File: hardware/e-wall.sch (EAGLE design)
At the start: 52 parts, among them IC1 74HCT595D, IC2 74HCT595D, IC3 74HCT595D, Q1 BSS123, Q10 BSS123, Q11 BSS123, Q12 BSS123, Q13 BSS123, Q14 BSS123, Q15 BSS123, Q16 BSS123, Q17 BSS123, Q18 BSS123, Q19 BSS123, Q2 BSS123, Q20 BSS123, Q21 BSS123, Q22 BSS123, Q23 BSS123, Q24 BSS123, Q3 BSS123, Q4 BSS123, Q5 BSS123, Q6 BSS123, Q7 BSS123, Q8 BSS123, Q9 BSS123

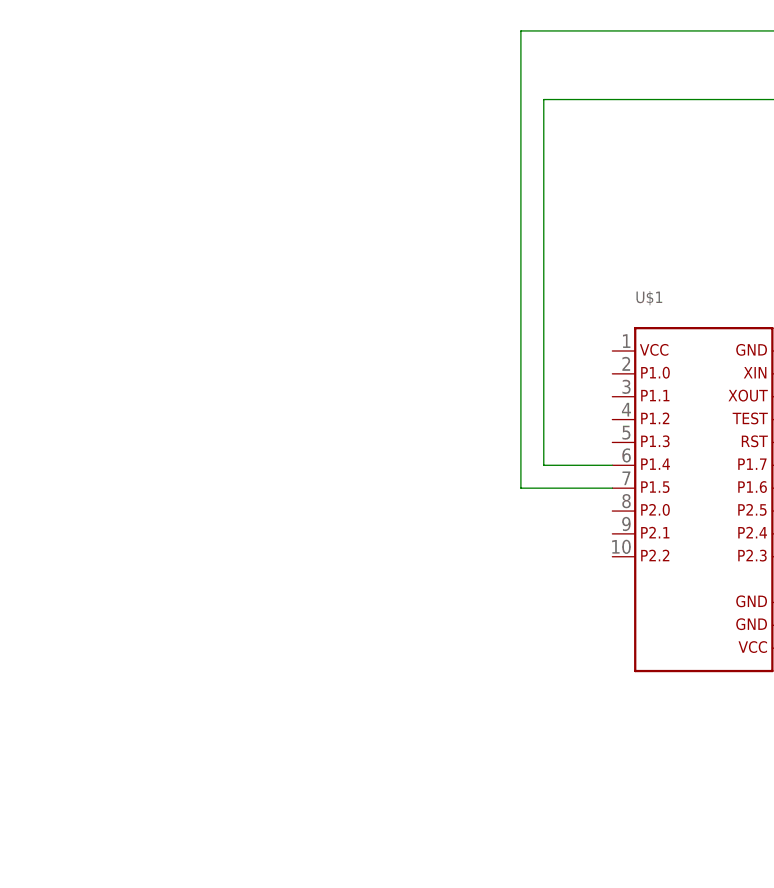
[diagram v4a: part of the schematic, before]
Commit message: Pegelwandler für Ultraschallsensor gezeichnet, aber noch nicht dimensioniert
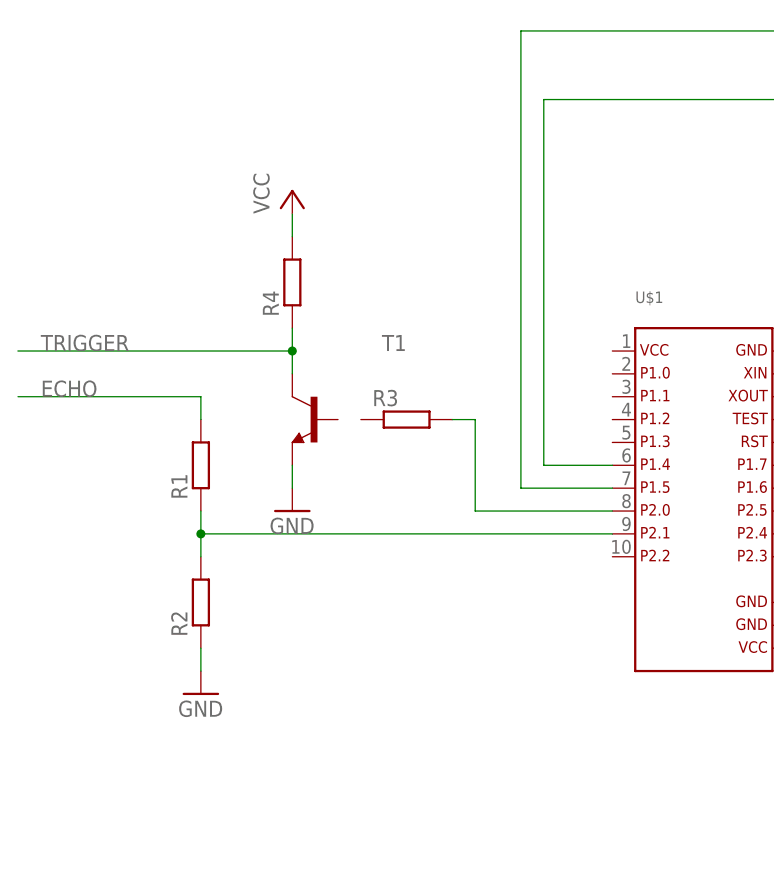
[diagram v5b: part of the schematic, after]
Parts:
- added R1, R2, R3, R4: (no value), resistor:R-EU_R0805
- added T1: (no value), transistor:-NPN-SOT23-EBC
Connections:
- new net ECHO: R1.2
- new net N$31: R1.1, R2.2, U$1.9
- new net N$32: R3.2, U$1.8
- new net TRIGGER: R4.1, T1.C
- net GND: now also R2.1, T1.E
- net VCC: now also R4.2
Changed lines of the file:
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@@
 <part name="P+26" library="supply1" deviceset="+12V" device=""/>
 <part name="P+27" library="supply1" deviceset="+12V" device=""/>
+<part name="R1" library="resistor" deviceset="R-EU_" device="R0805"/>
+<part name="R2" library="resistor" deviceset="R-EU_" device="R0805"/>
+<part name="R3" library="resistor" deviceset="R-EU_" device="R0805"/>
+<part name="R4" library="resistor" deviceset="R-EU_" device="R0805"/>
+<part name="T1" library="transistor" deviceset="*-NPN-" device="SOT23-EBC"/>
+<part name="GND28" library="supply1" deviceset="GND" device=""/>
+<part name="GND29" library="supply1" deviceset="GND" device=""/>
+<part name="P+28" library="supply1" deviceset="VCC" device=""/>
 </parts>
 <sheets>
@@
 <instance part="P+26" gate="1" x="447.04" y="68.58"/>
 <instance part="P+27" gate="1" x="447.04" y="43.18"/>
+<instance part="R1" gate="G$1" x="22.86" y="60.96" rot="R90"/>
+<instance part="R2" gate="G$1" x="22.86" y="45.72" rot="R90"/>
+<instance part="R3" gate="G$1" x="45.72" y="66.04"/>
+<instance part="R4" gate="G$1" x="33.02" y="81.28" rot="R90"/>
+<instance part="T1" gate="G$1" x="35.56" y="66.04" rot="MR0"/>
+<instance part="GND28" gate="1" x="33.02" y="55.88"/>
+<instance part="GND29" gate="1" x="22.86" y="35.56"/>
+<instance part="P+28" gate="VCC" x="33.02" y="91.44"/>
 </instances>
 <busses>
@@
 <pinref part="GND24" gate="1" pin="GND"/>
 <wire x1="439.42" y1="17.78" x2="439.42" y2="20.32" width="0.1524" layer="91"/>
+</segment>
+<segment>
+<pinref part="R2" gate="G$1" pin="1"/>
+<pinref part="GND29" gate="1" pin="GND"/>
+<wire x1="22.86" y1="40.64" x2="22.86" y2="38.1" width="0.1524" layer="91"/>
+</segment>
+<segment>
+<pinref part="T1" gate="G$1" pin="E"/>
+<pinref part="GND28" gate="1" pin="GND"/>
+<wire x1="33.02" y1="58.42" x2="33.02" y2="60.96" width="0.1524" layer="91"/>
 </segment>
 </net>
@@
 <pinref part="P+3" gate="VCC" pin="VCC"/>
 </segment>
+<segment>
+<pinref part="P+28" gate="VCC" pin="VCC"/>
+<pinref part="R4" gate="G$1" pin="2"/>
+<wire x1="33.02" y1="88.9" x2="33.02" y2="86.36" width="0.1524" layer="91"/>
+</segment>
 </net>
 <net name="OUT0" class="0">
@@
 </segment>
 </net>
+<net name="N$31" class="0">
+<segment>
+<pinref part="R1" gate="G$1" pin="1"/>
+<pinref part="R2" gate="G$1" pin="2"/>
+<wire x1="22.86" y1="55.88" x2="22.86" y2="53.34" width="0.1524" layer="91"/>
+<pinref part="U$1" gate="G$1" pin="9"/>
+<wire x1="22.86" y1="53.34" x2="22.86" y2="50.8" width="0.1524" layer="91"/>
+<wire x1="22.86" y1="53.34" x2="68.58" y2="53.34" width="0.1524" layer="91"/>
+<junction x="22.86" y="53.34"/>
+</segment>
+</net>
+<net name="N$32" class="0">
+<segment>
+<pinref part="U$1" gate="G$1" pin="8"/>
+<wire x1="68.58" y1="55.88" x2="53.34" y2="55.88" width="0.1524" layer="91"/>
+<wire x1="53.34" y1="55.88" x2="53.34" y2="66.04" width="0.1524" layer="91"/>
+<pinref part="R3" gate="G$1" pin="2"/>
+<wire x1="53.34" y1="66.04" x2="50.8" y2="66.04" width="0.1524" layer="91"/>
+</segment>
+</net>
+<net name="TRIGGER" class="0">
+<segment>
+<pinref part="T1" gate="G$1" pin="C"/>
+<pinref part="R4" gate="G$1" pin="1"/>
+<wire x1="33.02" y1="71.12" x2="33.02" y2="73.66" width="0.1524" layer="91"/>
+<wire x1="33.02" y1="73.66" x2="33.02" y2="76.2" width="0.1524" layer="91"/>
+<wire x1="33.02" y1="73.66" x2="2.54" y2="73.66" width="0.1524" layer="91"/>
+<junction x="33.02" y="73.66"/>
+<label x="5.08" y="73.66" size="1.778" layer="95"/>
+</segment>
+</net>
+<net name="ECHO" class="0">
+<segment>
+<pinref part="R1" gate="G$1" pin="2"/>
+<wire x1="22.86" y1="66.04" x2="22.86" y2="68.58" width="0.1524" layer="91"/>
+<wire x1="22.86" y1="68.58" x2="2.54" y2="68.58" width="0.1524" layer="91"/>
+<label x="5.08" y="68.58" size="1.778" layer="95"/>
+</segment>
+</net>

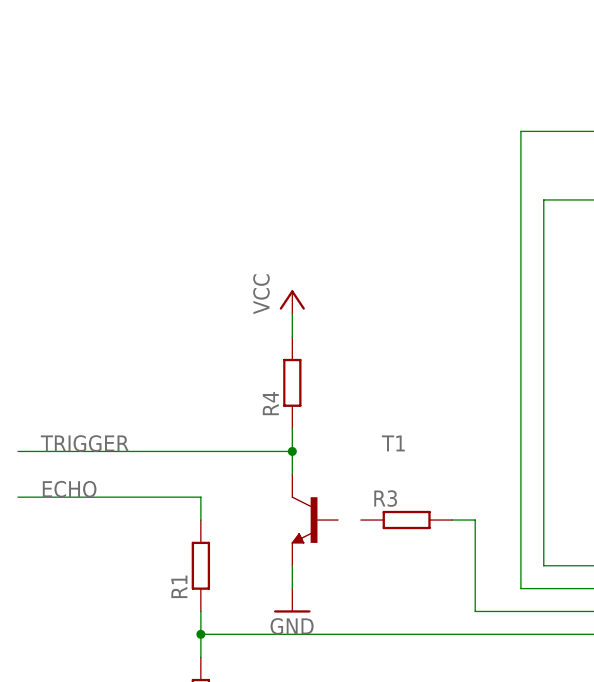
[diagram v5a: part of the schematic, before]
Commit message: Pegelwandler mit zwei Transistoren
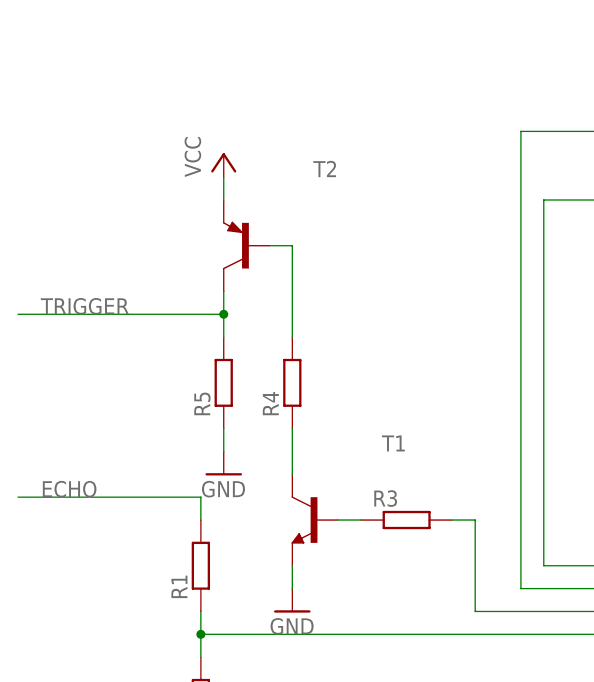
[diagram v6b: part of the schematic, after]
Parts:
- added R5: (no value), resistor:R-EU_R0805
- added T2: (no value), transistor:-PNP-SOT23-EBC
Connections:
- new net N$33: R3.1, T1.B
- new net N$34: R4.1, T1.C
- new net N$35: R4.2, T2.B
- net GND: now also R5.1
- net TRIGGER: now also R5.2, T2.C; no longer R4.1, T1.C
- net VCC: now also T2.E; no longer R4.2
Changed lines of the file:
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@@
 <part name="GND29" library="supply1" deviceset="GND" device=""/>
 <part name="P+28" library="supply1" deviceset="VCC" device=""/>
+<part name="T2" library="transistor" deviceset="*-PNP-" device="SOT23-EBC"/>
+<part name="R5" library="resistor" deviceset="R-EU_" device="R0805"/>
+<part name="GND30" library="supply1" deviceset="GND" device=""/>
 </parts>
 <sheets>
@@
 <instance part="GND28" gate="1" x="33.02" y="55.88"/>
 <instance part="GND29" gate="1" x="22.86" y="35.56"/>
-<instance part="P+28" gate="VCC" x="33.02" y="91.44"/>
+<instance part="P+28" gate="VCC" x="25.4" y="106.68"/>
+<instance part="T2" gate="G$1" x="27.94" y="96.52" rot="MR0"/>
+<instance part="R5" gate="G$1" x="25.4" y="81.28" rot="R90"/>
+<instance part="GND30" gate="1" x="25.4" y="71.12"/>
 </instances>
 <busses>
@@
 <pinref part="GND28" gate="1" pin="GND"/>
 <wire x1="33.02" y1="58.42" x2="33.02" y2="60.96" width="0.1524" layer="91"/>
+</segment>
+<segment>
+<pinref part="R5" gate="G$1" pin="1"/>
+<pinref part="GND30" gate="1" pin="GND"/>
+<wire x1="25.4" y1="76.2" x2="25.4" y2="73.66" width="0.1524" layer="91"/>
 </segment>
 </net>
@@
 <segment>
 <pinref part="P+28" gate="VCC" pin="VCC"/>
-<pinref part="R4" gate="G$1" pin="2"/>
-<wire x1="33.02" y1="88.9" x2="33.02" y2="86.36" width="0.1524" layer="91"/>
+<pinref part="T2" gate="G$1" pin="E"/>
+<wire x1="25.4" y1="104.14" x2="25.4" y2="101.6" width="0.1524" layer="91"/>
 </segment>
 </net>
@@
 </segment>
 </net>
-<net name="TRIGGER" class="0">
-<segment>
-<pinref part="T1" gate="G$1" pin="C"/>
-<pinref part="R4" gate="G$1" pin="1"/>
-<wire x1="33.02" y1="71.12" x2="33.02" y2="73.66" width="0.1524" layer="91"/>
-<wire x1="33.02" y1="73.66" x2="33.02" y2="76.2" width="0.1524" layer="91"/>
-<wire x1="33.02" y1="73.66" x2="2.54" y2="73.66" width="0.1524" layer="91"/>
-<junction x="33.02" y="73.66"/>
-<label x="5.08" y="73.66" size="1.778" layer="95"/>
-</segment>
-</net>
 <net name="ECHO" class="0">
 <segment>
@@
 </segment>
 </net>
+<net name="N$33" class="0">
+<segment>
+<pinref part="T1" gate="G$1" pin="B"/>
+<pinref part="R3" gate="G$1" pin="1"/>
+<wire x1="38.1" y1="66.04" x2="40.64" y2="66.04" width="0.1524" layer="91"/>
+</segment>
+</net>
+<net name="N$34" class="0">
+<segment>
+<pinref part="R4" gate="G$1" pin="1"/>
+<pinref part="T1" gate="G$1" pin="C"/>
+<wire x1="33.02" y1="76.2" x2="33.02" y2="71.12" width="0.1524" layer="91"/>
+</segment>
+</net>
+<net name="N$35" class="0">
+<segment>
+<pinref part="T2" gate="G$1" pin="B"/>
+<pinref part="R4" gate="G$1" pin="2"/>
+<wire x1="30.48" y1="96.52" x2="33.02" y2="96.52" width="0.1524" layer="91"/>
+<wire x1="33.02" y1="96.52" x2="33.02" y2="86.36" width="0.1524" layer="91"/>
+</segment>
+</net>
+<net name="TRIGGER" class="0">
+<segment>
+<pinref part="T2" gate="G$1" pin="C"/>
+<pinref part="R5" gate="G$1" pin="2"/>
+<wire x1="25.4" y1="91.44" x2="25.4" y2="88.9" width="0.1524" layer="91"/>
+<wire x1="25.4" y1="88.9" x2="25.4" y2="86.36" width="0.1524" layer="91"/>
+<wire x1="25.4" y1="88.9" x2="2.54" y2="88.9" width="0.1524" layer="91"/>
+<junction x="25.4" y="88.9"/>
+<label x="5.08" y="88.9" size="1.778" layer="95"/>
+</segment>
+</net>

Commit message: Launchpad angeschrieben
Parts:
- U$1: value (none) -> Launchpad
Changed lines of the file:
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@@
 <setting verticaltext="up"/>
 </settings>
-<grid distance="0.1" unitdist="inch" unit="inch" style="dots" multiple="1" display="yes" altdistance="0.01" altunitdist="inch" altunit="inch"/>
+<grid distance="0.1" unitdist="inch" unit="inch" style="lines" multiple="1" display="no" altdistance="0.01" altunitdist="inch" altunit="inch"/>
 <layers>
 <layer number="1" name="Top" color="4" fill="1" visible="no" active="no"/>
@@
 <layer number="91" name="Nets" color="2" fill="1" visible="yes" active="yes"/>
 <layer number="92" name="Busses" color="1" fill="1" visible="yes" active="yes"/>
-<layer number="93" name="Pins" color="2" fill="1" visible="yes" active="yes"/>
+<layer number="93" name="Pins" color="2" fill="1" visible="no" active="yes"/>
 <layer number="94" name="Symbols" color="4" fill="1" visible="yes" active="yes"/>
 <layer number="95" name="Names" color="7" fill="1" visible="yes" active="yes"/>
@@
 </classes>
 <parts>
-<part name="U$1" library="msp430launchpad" deviceset="MSP430LAUNCHPAD_FULL" device=""/>
+<part name="U$1" library="msp430launchpad" deviceset="MSP430LAUNCHPAD_FULL" device="" value="Launchpad"/>
 <part name="IC1" library="74xx-eu" deviceset="74*595" device="D" technology="HCT" value="74HCT595D"/>
 <part name="IC2" library="74xx-eu" deviceset="74*595" device="D" technology="HCT" value="74HCT595D"/>

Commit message: Werte für Spannungsteiler
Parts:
- R1: value (none) -> 20k
- R2: value (none) -> 30k
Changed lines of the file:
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@@
 <part name="P+26" library="supply1" deviceset="+12V" device=""/>
 <part name="P+27" library="supply1" deviceset="+12V" device=""/>
-<part name="R1" library="resistor" deviceset="R-EU_" device="R0805"/>
-<part name="R2" library="resistor" deviceset="R-EU_" device="R0805"/>
+<part name="R1" library="resistor" deviceset="R-EU_" device="R0805" value="20k"/>
+<part name="R2" library="resistor" deviceset="R-EU_" device="R0805" value="30k"/>
 <part name="R3" library="resistor" deviceset="R-EU_" device="R0805"/>
 <part name="R4" library="resistor" deviceset="R-EU_" device="R0805"/>
